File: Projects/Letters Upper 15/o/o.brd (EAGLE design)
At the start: 16.5 x 21.6 mm, 42 parts

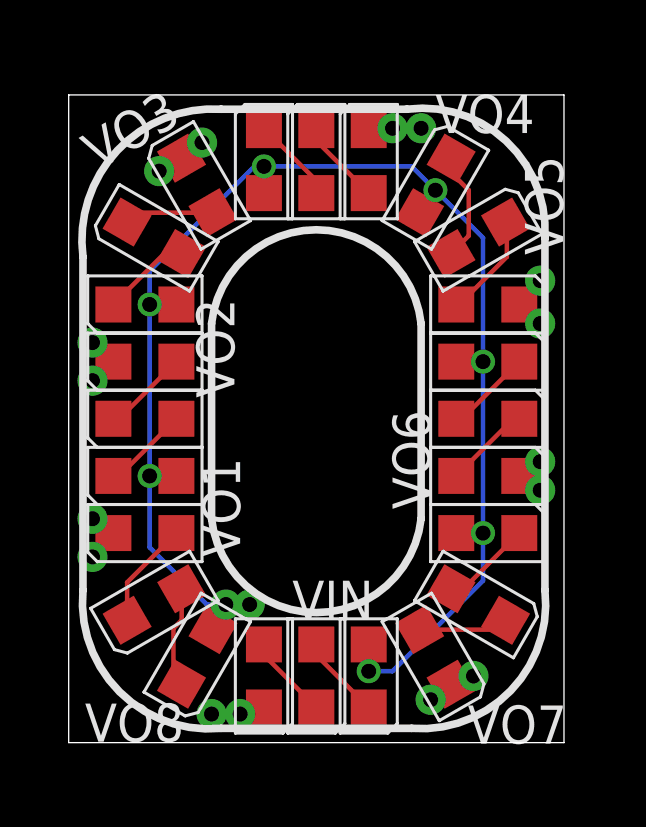
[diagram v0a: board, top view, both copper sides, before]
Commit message: 
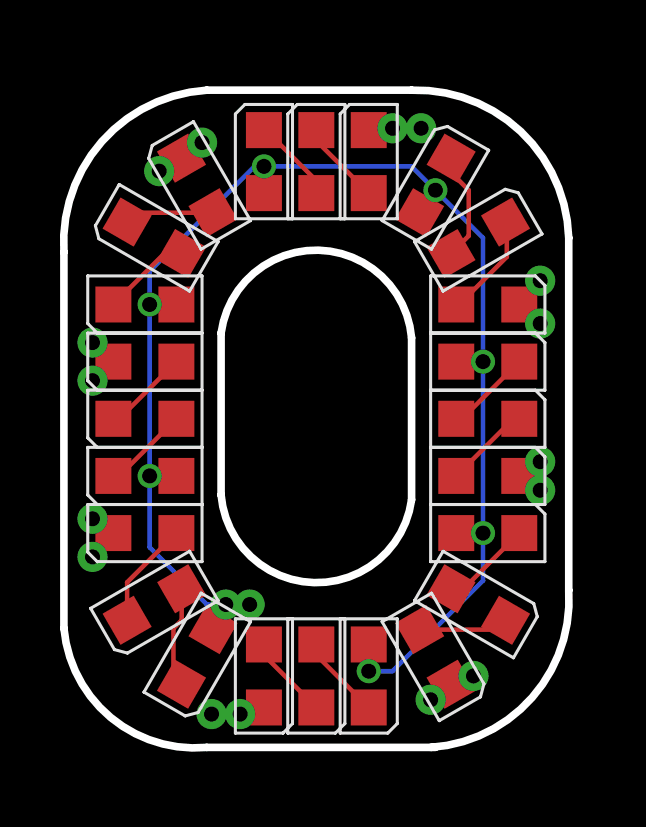
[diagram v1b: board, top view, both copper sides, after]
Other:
- board size 16.5 x 21.6 mm -> 16.8 x 21.9 mm
